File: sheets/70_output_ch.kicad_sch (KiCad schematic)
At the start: 17 parts, among them Q701 FDD7N25LZ, Q702 BC817-40, Q703 BC807-40

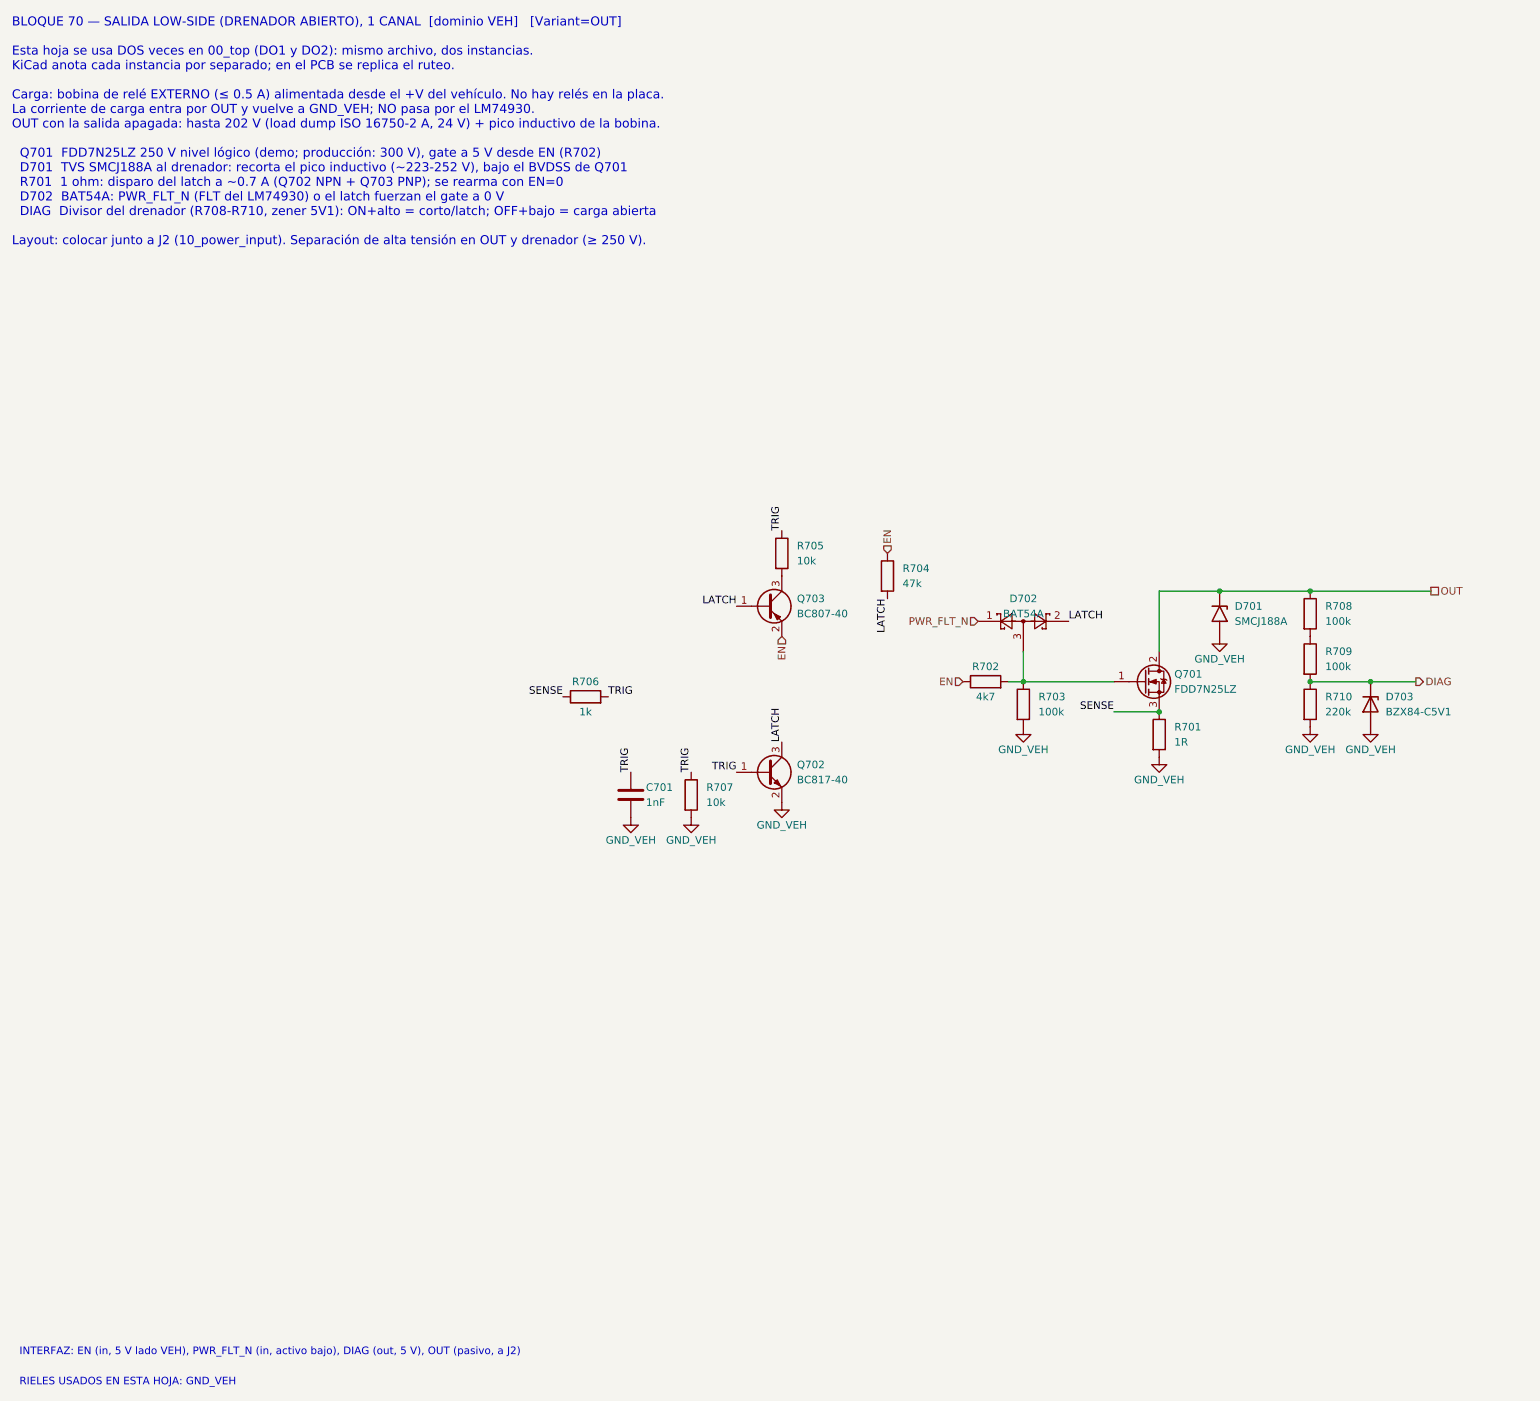
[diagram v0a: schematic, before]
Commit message: [Claude Code] 60_can, 70_output, 10_power_input: criterio prototipo = producción, campo DNP
- 60_can: ADM3055E según datasheet Rev. D (tabla 10): FB602 separa GNDISO
  de GND2, VISOOUT con 0.22 uF + 10 uF, RS a GND2 por R605 (0 ohm), AUXIN a
  GND1, pull-up de STBY, ESD2CAN24-Q1 DNP; referencias 6xx y campos completos.
- 70_output: DMN10H220LQ (100 V, SOT-23), SMAJ58A, buffer 74AHCT1G126
  (3.3 -> 5 V), zener de gate; latch y diagnóstico como huellas DNP.
- 10_power_input: J1/J2 MSTB 2,5 de 5.08 mm GF (J2 = 1776508), F101
  SF-2410FPA200W-2, C105 hold-up DNP; se quita un PWR_FLAG suelto en GND_CAN.
- Campo DNP (vacío / PROTO / PROD / PROTO,PROD) en todos los símbolos.
- README y PENDIENTES: decisiones del usuario, máximos de la entrada,
  temas abiertos (buck de la opción B, R109, TVS de entrada grande).

Co-Authored-By: Claude Opus 5.5 <noreply@anthropic.com>
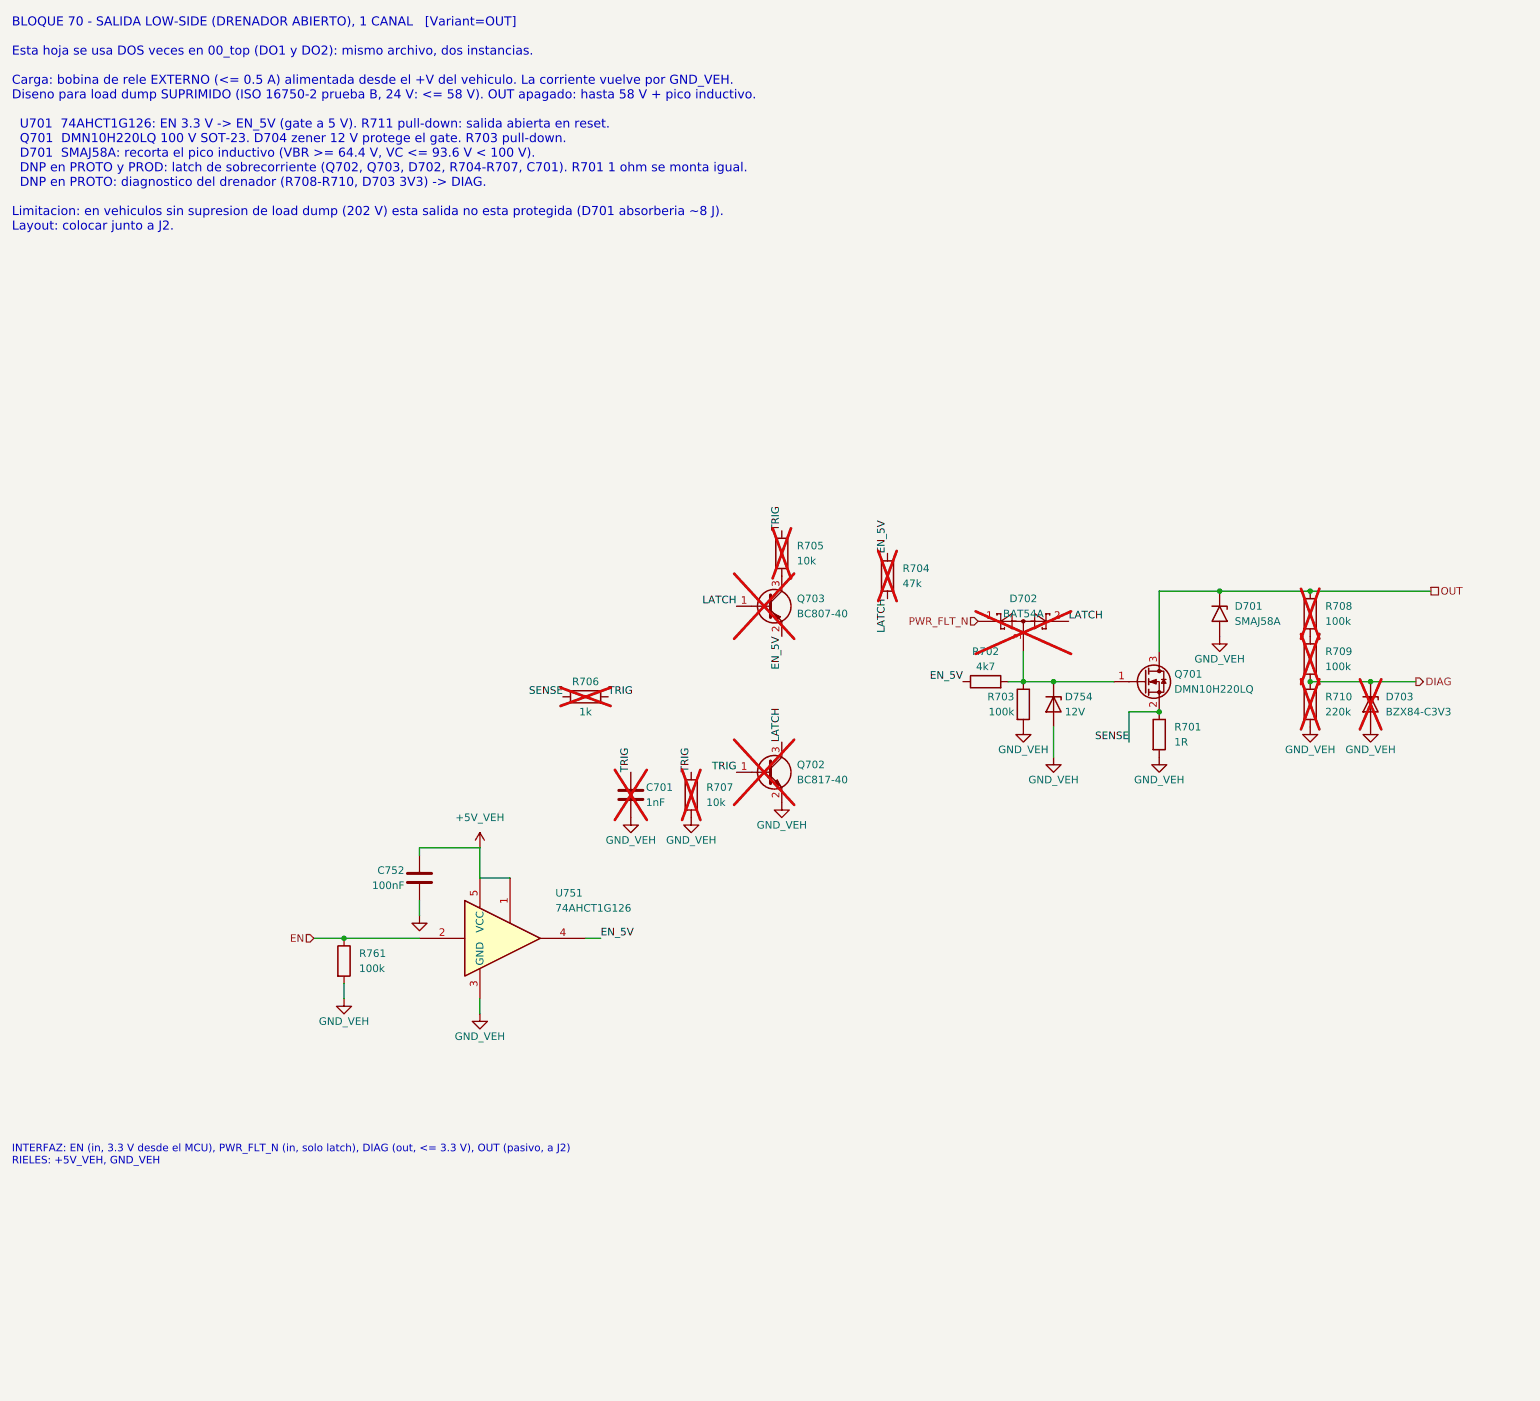
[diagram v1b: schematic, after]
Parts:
- added C752: 100nF, Capacitor_SMD:C_0603_1608Metric, symbol Device:C
- added D754: 12V, Diode_SMD:D_SOD-123, symbol Device:D_Zener
- added R761: 100k, Resistor_SMD:R_0603_1608Metric, symbol Device:R
- added U751: 74AHCT1G126, Package_TO_SOT_SMD:SOT-23-5, symbol 74xGxx:74AHCT1G126
- C701, D702, Q702, Q703, R704, R705, R706, R707: DNP (none) -> PROTO,PROD; Notes (none) -> Latch de sobrecorriente: huella reservada, DNP hasta valida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; now not fitted
- D701: value SMCJ188A -> SMAJ58A; footprint Diode_SMD:D_SMC -> Diode_SMD:D_SMA; symbol Diode:SM6T200A -> Diode:SMAJ58A; MPN SMCJ188A -> SMAJ58A; Notes Recorta el pico inductivo de la bobina externa: ~223-252 V 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 -> Recorta el pico inductivo del rele: VBR 64.4-71.2 V (no con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
- D703: value BZX84-C5V1 -> BZX84-C3V3; DNP (none) -> PROTO; MPN BZX84-C5V1,215 -> BZX84-C3V3,215; Notes (none) -> Diagnostico (DNP en prototipo): limita DIAG a 3.3 V para el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; now not fitted
- Q701: value FDD7N25LZ -> DMN10H220LQ; footprint Package_TO_SOT_SMD:TO-252-2 -> Package_TO_SOT_SMD:SOT-23; symbol Transistor_FET:IPD50R380CE -> Transistor_FET:DMN10H220L; Alt_MPN (none) -> DMN10H220L-7; MPN FDD7N25LZTM -> DMN10H220LQ-7; Manufacturer onsemi -> Diodes Incorporated; Notes DEMO, NO es AEC-Q101 (el datasheet onsemi/Fairchild Rev 1.5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 -> 100 V, RDS(on) 250 mohm max a VGS 4.5 V, 1.3 A. AEC-Q101. G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
- R701: Notes 1206 anti-surge en vez de 0603: 0.25 W a 0.5 A y pulsos de 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 -> Shunt del latch (DNP). Se monta siempre: con el latch sin m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
- R702: Notes (none) -> Gate en serie: limita la corriente de carga del gate y deja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
- R703: Notes (none) -> Pull-down de gate: Q701 apagado sin +5V_VEH.
- R708, R709, R710: DNP (none) -> PROTO; now not fitted
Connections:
- net EN: now also R761.1, U751.2; no longer Q703.2 (E), R702.1, R704.1
- net GND_VEH: now also C752.2, D754.2 (A), R761.2, U751.3 (GND)
- net OUT: now also Q701.3 (D); no longer Q701.2 (D)
- net SENSE: now also Q701.2 (S); no longer Q701.3 (S)
- net at D702.3, Q701.1 (G), R702.2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: now also D754.1 (K)
- new net +5V_VEH: C752.1, U751.1, U751.5 (VCC)
- new net EN_5V: Q703.2 (E), R702.1, R704.1, U751.4
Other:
- note added: "BLOQUE 70 - SALIDA LOW-SIDE (DRENADOR ABIERTO), 1 CANAL [Variant=OUT] Esta hoja se usa DOS veces en 00_top (DO1 y DO2): mismo archivo, dos instancias. Carga: bobina de rele EXTERNO (<= 0.5 A) alimentada desde el +V del vehiculo. La corriente vuelve por GND_VEH. Diseno para load dump SUPRIMIDO (ISO 16750-2 prueba B, 24 V: <= 58 V). OUT apagado: hasta 58 V + pico inductivo. U701 74AHCT1G126: EN 3.3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"
- note added: "INTERFAZ: EN (in, 3.3 V desde el MCU), PWR_FLT_N (in, solo latch), DIAG (out, <= 3.3 V), OUT (pasivo, a J2) RIELES: +5V_VEH, GND_VEH"
- note removed: "BLOQUE 70 — SALIDA LOW-SIDE (DRENADOR ABIERTO), 1 CANAL [dominio VEH] [Variant=OUT] Esta hoja se usa DOS veces en 00_top (DO1 y DO2): mismo archivo, dos instancias. KiCad anota cada instancia por separado; en el PCB se replica el ruteo. Carga: bobina de relé EXTERNO (≤ 0.5 A) alimentada desde el +V del vehículo. No hay relés en la placa. La corriente de carga entra por OUT y vuelve a GND_VEH; NO 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"
- note removed: "INTERFAZ: EN (in, 5 V lado VEH), PWR_FLT_N (in, activo bajo), DIAG (out, 5 V), OUT (pasivo, a J2)"
- note removed: "RIELES USADOS EN ESTA HOJA: GND_VEH"

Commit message: [Claude Code] 20_buck_5v: opción B (no aislada) con LMR38010; masas unificadas
- sheets/20_isolation -> sheets/20_buck_5v: se quitan PS201, ISO7763 y
  TPS7A1650; U201 LMR38010SQDDARQ1 (PROTO: LMR38010SDDAR, LCSC C5219310),
  5.02 V / 1 A a 400 kHz según TI SNVSC73B (L201 XAL6060-333, 3 x 22 uF,
  RT 64.9k, FB 100k/24.9k). Huella oficial HSOIC-8 con vías térmicas.
- Símbolo LMR38010 (easyeda2kicad) en lib/easyeda2kicad/INCLI-VA_easyeda,
  con tipos de pin ajustados; registrado en sym-lib-table.
- Todas las hojas: GND_ISO -> GND_VEH, +5V_ISO -> +5V_VEH.
- Raíz: EN/DIAG/FLT directos entre las hojas 40, 70 y 10; la hoja 20 sin pines.
- 10_power_input: R111 a +3V3_D, C109 = 100 nF (inrush con C105),
  C105 DNP solo en PROTO; se quita un PWR_FLAG suelto en GND_VEH.
- 70_output_ch: cambios de layout del usuario (hechos en KiCad).
- Textos de las hojas 30/40/50/80 y la raíz sin referencias al aislamiento.
- ERC: 0 en 10, 20, 30, 40, 50, 60 y 70; quedan los de 80 (hoja vacía).

Co-Authored-By: Claude Opus 5.5 <noreply@anthropic.com>
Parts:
- renumbered C752 to C702, D754 to D704, R761 to R711, U751 to U701
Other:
- moved on the sheet: C701, C702, D701, D702, D703, D704, Q701, Q702, Q703, R701, R702, R703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
